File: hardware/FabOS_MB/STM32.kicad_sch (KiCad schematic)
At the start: 38 parts, among them J601 Conn_ST_STDC14, SW601 boot, SW602 SW_Push, SW603 SW_Push, SW604 SW_Push, SW605 SW_Push, U601 STM32F407VETx

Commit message: update components placement
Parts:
- SW601, SW602: footprint Button_Switch_SMD:SW_Push_1P1T_NO_6x6mm_H9.5mm -> Button_Switch_SMD:SW_SPST_B3U-3000P
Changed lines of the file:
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@@
 			)
 		)
-		(property "Footprint" "Button_Switch_SMD:SW_Push_1P1T_NO_6x6mm_H9.5mm"
+		(property "Footprint" "Button_Switch_SMD:SW_SPST_B3U-3000P"
 			(at 17.78 40.64 0)
 			(effects
@@
 			)
 		)
-		(property "Footprint" "Button_Switch_SMD:SW_Push_1P1T_NO_6x6mm_H9.5mm"
+		(property "Footprint" "Button_Switch_SMD:SW_SPST_B3U-3000P"
 			(at 143.51 58.42 0)
 			(effects

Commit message: update pcb
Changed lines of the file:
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@@
 		(lib_id "power:GND")
 		(at 261.62 33.02 0)
+		(mirror y)
 		(unit 1)
 		(exclude_from_sim no)
@@
 		(on_board yes)
 		(dnp no)
-		(fields_autoplaced yes)
 		(property "Reference" "#PWR0625"
 			(at 261.62 39.37 0)

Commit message: update pcb
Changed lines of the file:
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@@
 		(lib_id "Device:C_Small")
 		(at 162.56 58.42 0)
+		(mirror y)
 		(unit 1)
 		(exclude_from_sim no)
@@
 		(on_board yes)
 		(dnp no)
-		(fields_autoplaced yes)
 		(property "Reference" "C605"
-			(at 165.1 57.1562 0)
+			(at 160.02 57.1562 0)
 			(effects
 				(font
@@
 		)
 		(property "Value" "100n"
-			(at 165.1 59.6962 0)
+			(at 160.02 59.6962 0)
 			(effects
 				(font

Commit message: Modification PCB
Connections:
- net USB_OTG_DM renamed USB_OTG_D-
- net USB_OTG_FS_DP renamed USB_OTG_D+
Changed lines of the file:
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@@
 		)
 	)
-	(hierarchical_label "USB_OTG_DM"
+	(hierarchical_label "USB_OTG_D-"
 		(shape bidirectional)
 		(at 99.06 68.58 0)
@@
 		)
 	)
-	(hierarchical_label "USB_OTG_FS_DP"
+	(hierarchical_label "USB_OTG_D+"
 		(shape bidirectional)
 		(at 99.06 71.12 0)

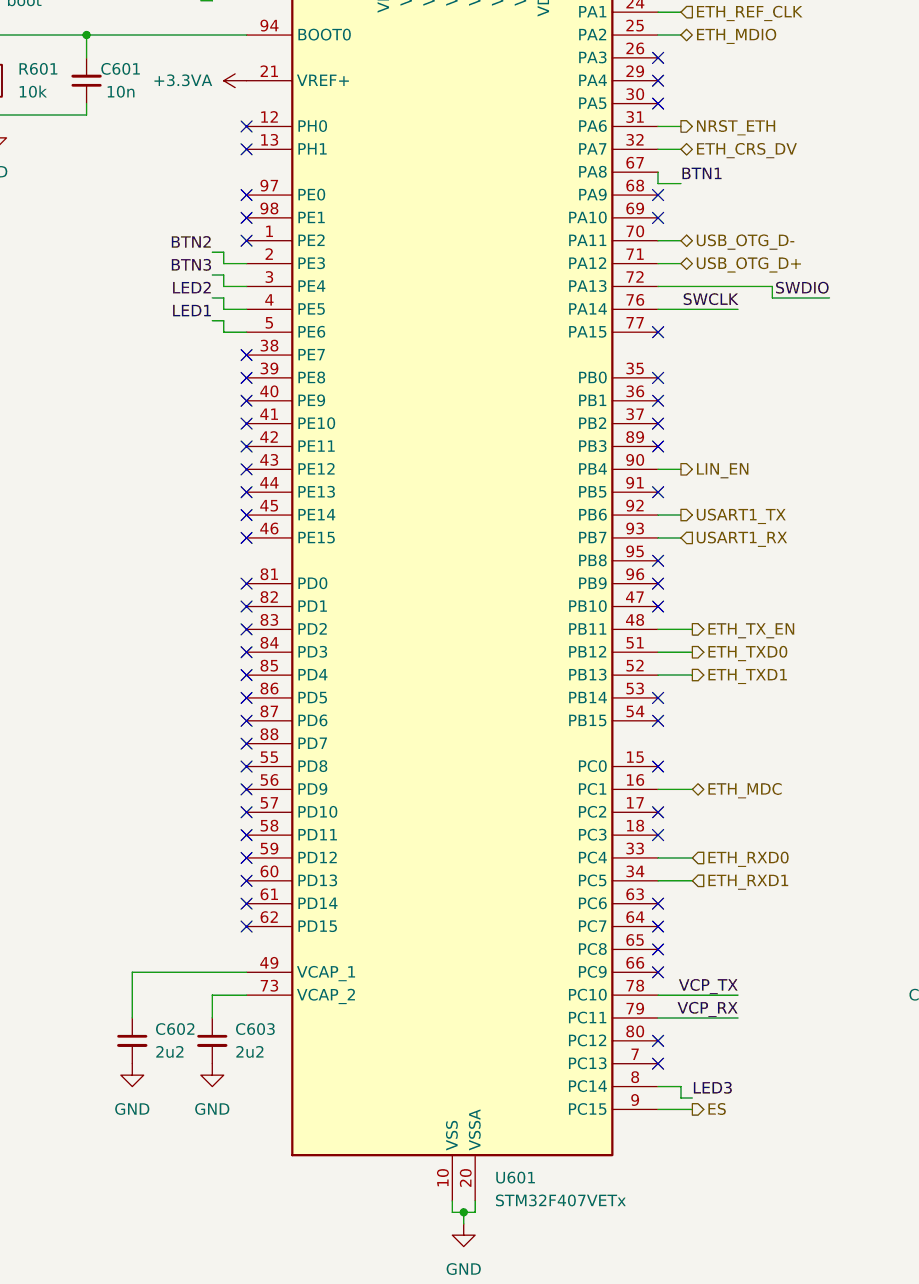
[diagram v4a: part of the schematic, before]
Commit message: update pcb routing
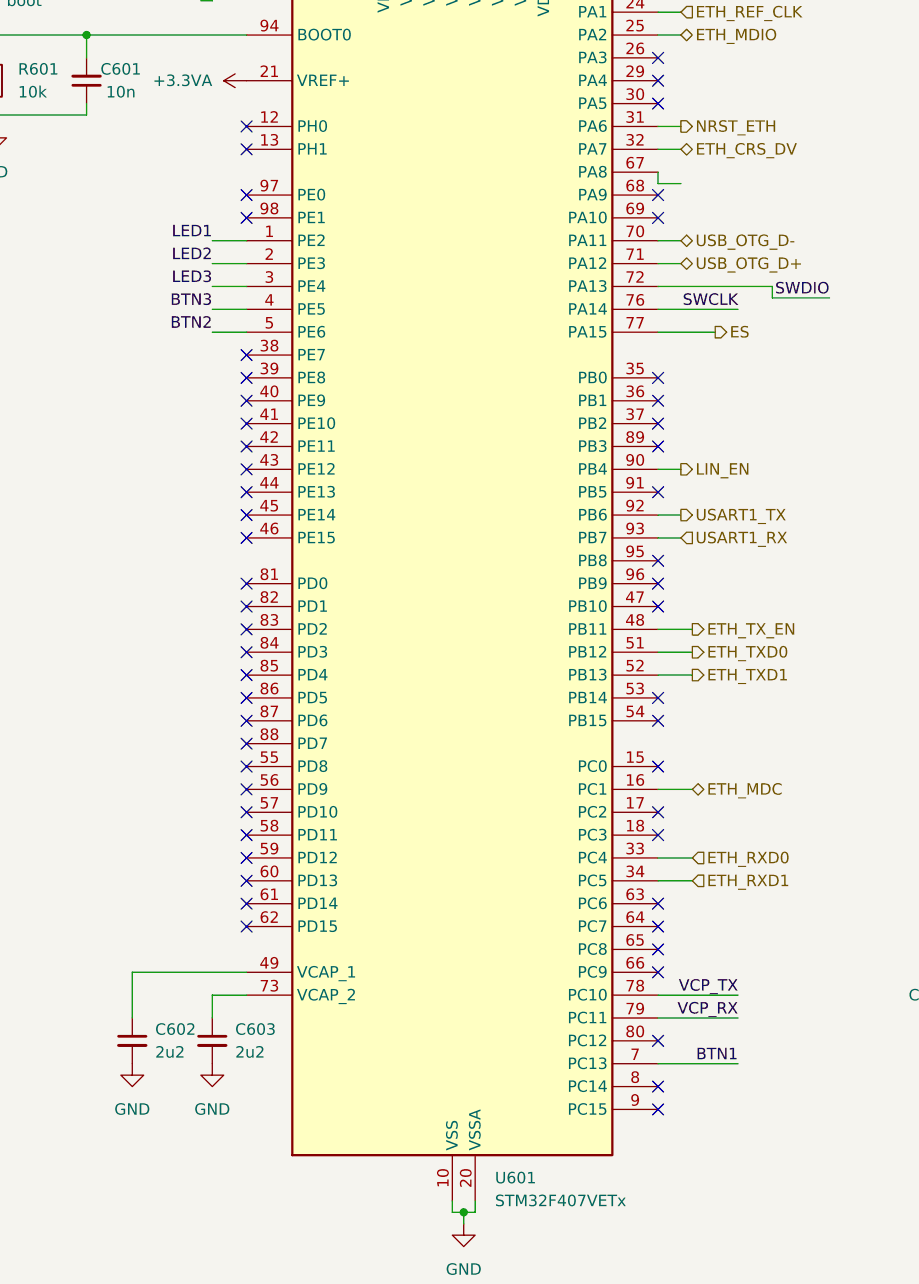
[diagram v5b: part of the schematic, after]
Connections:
- net BTN1: now also U601.7 (PC13); no longer U601.67 (PA8)
- net BTN2: now also U601.5 (PE6); no longer U601.2 (PE3)
- net BTN3: now also U601.4 (PE5); no longer U601.3 (PE4)
- net ES: now also U601.77 (PA15); no longer U601.9 (PC15)
- net LED1: now also U601.1 (PE2); no longer U601.5 (PE6)
- net LED2: now also U601.2 (PE3); no longer U601.4 (PE5)
- net LED3: now also U601.3 (PE4); no longer U601.8 (PC14)
- no-connect marks 59 -> 58
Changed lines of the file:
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@@
+	)
+	(no_connect
+		(at 96.52 162.56)
 	)
 	(no_connect
@@
 	)
 	(no_connect
+		(at 96.52 165.1)
+	)
+	(no_connect
 		(at 96.52 96.52)
 	)
@@
 	)
 	(no_connect
-		(at 96.52 78.74)
-	)
-	(no_connect
 		(at 50.8 58.42)
 	)
@@
 	)
 	(no_connect
-		(at 96.52 160.02)
-	)
-	(no_connect
 		(at 50.8 132.08)
 	)
@@
 	)
 	(no_connect
-		(at 50.8 68.58)
-	)
-	(no_connect
 		(at 50.8 119.38)
 	)
@@
 	(wire
 		(pts
-			(xy 48.26 71.12) (xy 50.8 71.12)
-		)
-		(stroke
-			(width 0)
-			(type default)
-		)
-	)
-	(wire
-		(pts
 			(xy 182.88 111.76) (xy 179.07 111.76)
 		)
@@
 	(wire
 		(pts
-			(xy 46.99 69.85) (xy 48.26 69.85)
+			(xy 46.99 71.12) (xy 50.8 71.12)
 		)
 		(stroke
@@
 	(wire
 		(pts
-			(xy 48.26 77.47) (xy 48.26 78.74)
-		)
-		(stroke
-			(width 0)
-			(type default)
-		)
-	)
-	(wire
-		(pts
-			(xy 48.26 69.85) (xy 48.26 71.12)
-		)
-		(stroke
-			(width 0)
-			(type default)
-		)
-	)
-	(wire
-		(pts
 			(xy 171.45 31.75) (xy 171.45 29.21)
 		)
@@
 	(wire
 		(pts
-			(xy 48.26 73.66) (xy 50.8 73.66)
-		)
-		(stroke
-			(width 0)
-			(type default)
-		)
-	)
-	(wire
-		(pts
-			(xy 100.33 165.1) (xy 96.52 165.1)
-		)
-		(stroke
-			(width 0)
-			(type default)
-		)
-	)
-	(wire
-		(pts
 			(xy 227.33 111.76) (xy 227.33 113.03)
 		)
@@
 	(wire
 		(pts
-			(xy 46.99 74.93) (xy 48.26 74.93)
+			(xy 46.99 76.2) (xy 50.8 76.2)
 		)
 		(stroke
@@
 	(wire
 		(pts
+			(xy 102.87 78.74) (xy 96.52 78.74)
+		)
+		(stroke
+			(width 0)
+			(type default)
+		)
+	)
+	(wire
+		(pts
 			(xy 66.04 29.21) (xy 68.58 29.21)
 		)
@@
 	(wire
 		(pts
-			(xy 100.33 163.83) (xy 99.06 163.83)
-		)
-		(stroke
-			(width 0)
-			(type default)
-		)
-	)
-	(wire
-		(pts
 			(xy 261.62 30.48) (xy 261.62 33.02)
 		)
@@
 	(wire
 		(pts
-			(xy 46.99 72.39) (xy 48.26 72.39)
+			(xy 46.99 73.66) (xy 50.8 73.66)
 		)
 		(stroke
@@
 	(wire
 		(pts
-			(xy 48.26 74.93) (xy 48.26 76.2)
-		)
-		(stroke
-			(width 0)
-			(type default)
-		)
-	)
-	(wire
-		(pts
 			(xy 22.86 45.72) (xy 33.02 45.72)
 		)
@@
 	(wire
 		(pts
+			(xy 105.41 160.02) (xy 96.52 160.02)
+		)
+		(stroke
+			(width 0)
+			(type default)
+		)
+	)
+	(wire
+		(pts
 			(xy 100.33 129.54) (xy 96.52 129.54)
 		)
@@
 	(wire
 		(pts
-			(xy 99.06 163.83) (xy 99.06 162.56)
-		)
-		(stroke
-			(width 0)
-			(type default)
-		)
-	)
-	(wire
-		(pts
 			(xy 148.59 170.18) (xy 149.86 170.18)
 		)
@@
 	(wire
 		(pts
-			(xy 46.99 77.47) (xy 48.26 77.47)
+			(xy 46.99 78.74) (xy 50.8 78.74)
 		)
 		(stroke
@@
 	(wire
 		(pts
-			(xy 48.26 78.74) (xy 50.8 78.74)
-		)
-		(stroke
-			(width 0)
-			(type default)
-		)
-	)
-	(wire
-		(pts
 			(xy 162.56 52.07) (xy 162.56 55.88)
 		)
@@
 	(wire
 		(pts
+			(xy 46.99 68.58) (xy 50.8 68.58)
+		)
+		(stroke
+			(width 0)
+			(type default)
+		)
+	)
+	(wire
+		(pts
 			(xy 232.41 31.75) (xy 232.41 33.02)
 		)
@@
 	(wire
 		(pts
-			(xy 99.06 162.56) (xy 96.52 162.56)
-		)
-		(stroke
-			(width 0)
-			(type default)
-		)
-	)
-	(wire
-		(pts
 			(xy 256.54 111.76) (xy 260.35 111.76)
 		)
@@
 	(wire
 		(pts
-			(xy 48.26 72.39) (xy 48.26 73.66)
-		)
-		(stroke
-			(width 0)
-			(type default)
-		)
-	)
-	(wire
-		(pts
 			(xy 161.29 31.75) (xy 171.45 31.75)
 		)
@@
 		(pts
 			(xy 163.83 163.83) (xy 175.26 163.83)
-		)
-		(stroke
-			(width 0)
-			(type default)
-		)
-	)
-	(wire
-		(pts
-			(xy 48.26 76.2) (xy 50.8 76.2)
 		)
 		(stroke
@@
 		)
 	)
+	(label "BTN1"
+		(at 105.41 160.02 180)
+		(fields_autoplaced yes)
+		(effects
+			(font
+				(size 1.27 1.27)
+			)
+			(justify right bottom)
+		)
+	)
 	(label "SWCLK"
 		(at 175.26 143.51 180)
@@
 		)
 	)
-	(label "LED2"
-		(at 46.99 74.93 180)
-		(fields_autoplaced yes)
-		(effects
-			(font
-				(size 1.27 1.27)
-			)
-			(justify right bottom)
-		)
-	)
 	(label "LED3"
 		(at 267.97 52.07 0)
@@
 		)
 	)
+	(label "LED3"
+		(at 46.99 73.66 180)
+		(fields_autoplaced yes)
+		(effects
+			(font
+				(size 1.27 1.27)
+			)
+			(justify right bottom)
+		)
+	)
 	(label "BTN1"
 		(at 167.64 111.76 0)
@@
 		)
 	)
-	(label "LED3"
-		(at 100.33 163.83 0)
-		(fields_autoplaced yes)
-		(effects
-			(font
-				(size 1.27 1.27)
-			)
-			(justify left bottom)
-		)
-	)
 	(label "SWDIO"
 		(at 115.57 74.93 180)
@@
 		)
 	)
+	(label "LED1"
+		(at 46.99 68.58 180)
+		(fields_autoplaced yes)
+		(effects
+			(font
+				(size 1.27 1.27)
+			)
+			(justify right bottom)
+		)
+	)
 	(label "BTN3"
-		(at 46.99 72.39 180)
+		(at 46.99 76.2 180)
 		(fields_autoplaced yes)
 		(effects
@@
 			)
 			(justify right bottom)
-		)
-	)
-	(label "BTN1"
-		(at 99.06 62.23 0)
-		(fields_autoplaced yes)
-		(effects
-			(font
-				(size 1.27 1.27)
-			)
-			(justify left bottom)
 		)
 	)
@@
 		)
 	)
-	(label "BTN2"
-		(at 46.99 69.85 180)
-		(fields_autoplaced yes)
-		(effects
-			(font
-				(size 1.27 1.27)
-			)
-			(justify right bottom)
-		)
-	)
 	(label "LED2"
 		(at 255.27 52.07 0)
@@
 		)
 	)
+	(label "LED2"
+		(at 46.99 71.12 180)
+		(fields_autoplaced yes)
+		(effects
+			(font
+				(size 1.27 1.27)
+			)
+			(justify right bottom)
+		)
+	)
+	(label "BTN2"
+		(at 46.99 78.74 180)
+		(fields_autoplaced yes)
+		(effects
+			(font
+				(size 1.27 1.27)
+			)
+			(justify right bottom)
+		)
+	)
 	(label "SWCLK"
 		(at 105.41 76.2 180)
-		(fields_autoplaced yes)
-		(effects
-			(font
-				(size 1.27 1.27)
-			)
-			(justify right bottom)
-		)
-	)
-	(label "LED1"
-		(at 46.99 77.47 180)
 		(fields_autoplaced yes)
 		(effects
@@
 		)
 	)
+	(hierarchical_label "ES"
+		(shape output)
+		(at 102.87 78.74 0)
+		(fields_autoplaced yes)
+		(effects
+			(font
+				(size 1.27 1.27)
+			)
+			(justify left)
+		)
+	)
 	(hierarchical_label "USB_OTG_D-"
 		(shape bidirectional)
@@
 		(fields_autoplaced yes)
 		(effects
-			(font
-				(size 1.27 1.27)
-			)
-			(justify left)
-		)
-	)
-	(hierarchical_label "ES"
-		(shape output)
-		(at 100.33 165.1 0)
-		(fields_autoplaced yes)
-		(effects

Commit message: update pcb
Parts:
- R606, R608, R610: value R_Small -> 1k5
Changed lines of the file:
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@@
 			)
 		)
-		(property "Value" "R_Small"
+		(property "Value" "1k5"
 			(at 245.11 60.9599 0)
 			(effects
@@
 			)
 		)
-		(property "Value" "R_Small"
+		(property "Value" "1k5"
 			(at 257.81 60.9599 0)
 			(effects
@@
 			)
 		)
-		(property "Value" "R_Small"
+		(property "Value" "1k5"
 			(at 270.51 60.9599 0)
 			(effects

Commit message: update pcb
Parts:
- SW601, SW602: LCSC (none) -> C963349; MPN (none) -> B3U-3000P
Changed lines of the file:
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@@
+			)
+		)
+		(property "MPN" " B3U-3000P"
+			(at 22.86 40.64 90)
+			(effects
+				(font
+					(size 1.27 1.27)
+				)
+				(hide yes)
+			)
+		)
+		(property "LCSC" " C963349"
+			(at 22.86 40.64 90)
+			(effects
+				(font
+					(size 1.27 1.27)
+				)
+				(hide yes)
 			)
 		)
@@
 			(effects
 				(font
+					(size 1.27 1.27)
+				)
+				(hide yes)
+			)
+		)
+		(property "MPN" "B3U-3000P"
+			(at 148.59 58.42 90)
+			(effects
+				(font
+					(size 1.27 1.27)
+				)
+				(hide yes)
+			)
+		)
+		(property "LCSC" " C963349"
+			(at 148.59 58.42 90)
+			(effects
+				(font

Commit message: MàJ BoM dans Kicad
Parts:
- C601, C608, C612, C616: LCSC (none) -> C576726
- C604, C605, C606, C607, C609, C610, C611, C614, C617: LCSC (none) -> C361203
- C615: LCSC (none) -> C113791
- J601: LCSC (none) -> C3975190
- R601, R602, R603, R604, R605, R607, R609: LCSC (none) -> C25744
- R606, R608, R610: LCSC (none) -> C114759
- SW603, SW604, SW605: LCSC (none) -> C5127964
- U601: LCSC (none) -> C390804
